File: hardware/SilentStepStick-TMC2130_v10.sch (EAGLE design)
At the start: 26 parts, among them IC1 TMC2100-LA, X1 PASSER-07, X2 PASSER-07

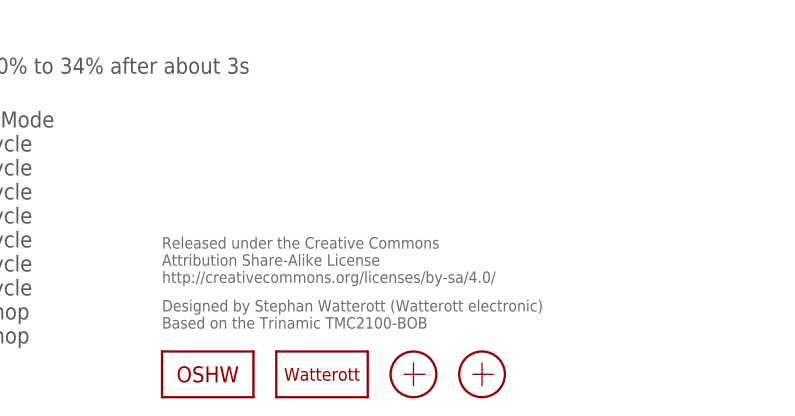
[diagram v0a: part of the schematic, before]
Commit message: updated schematics
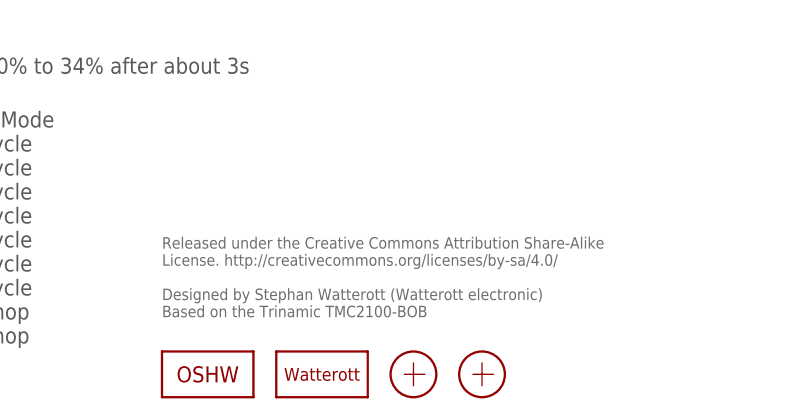
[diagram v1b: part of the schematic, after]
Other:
- note added: "Released under the Creative Commons Attribution Share-Alike License. http://creativecommons.org/licenses/by-sa/4.0/ Designed by Stephan Watterott (Watterott electronic) Based on the Trinamic TMC2100-BOB"
- note removed: "Designed by Stephan Watterott (Watterott electronic) Based on the Trinamic TMC2100-BOB"
- note removed: "Released under the Creative Commons Attribution Share-Alike License http://creativecommons.org/licenses/by-sa/4.0/"
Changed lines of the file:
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@@
 <setting verticaltext="up"/>
 </settings>
-<grid distance="0.1" unitdist="inch" unit="inch" style="lines" multiple="1" display="no" altdistance="0.01" altunitdist="inch" altunit="inch"/>
+<grid distance="0.05" unitdist="inch" unit="inch" style="lines" multiple="1" display="yes" altdistance="0.025" altunitdist="inch" altunit="inch"/>
 <layers>
 <layer number="1" name="Top" color="4" fill="1" visible="no" active="no"/>
@@
 <wire x1="38.1" y1="40.64" x2="38.1" y2="43.18" width="1.016" layer="94"/>
 <wire x1="38.1" y1="25.4" x2="38.1" y2="27.94" width="1.016" layer="94"/>
-<text x="162.56" y="17.78" size="1.27" layer="95">Released under the Creative Commons
-Attribution Share-Alike License
-http://creativecommons.org/licenses/by-sa/4.0/</text>
-<text x="162.56" y="12.7" size="1.27" layer="95">Designed by Stephan Watterott (Watterott electronic)
+<text x="162.56" y="22.86" size="1.27" layer="95" align="top-left">Released under the Creative Commons Attribution Share-Alike
+License. http://creativecommons.org/licenses/by-sa/4.0/
+Designed by Stephan Watterott (Watterott electronic)
 Based on the Trinamic TMC2100-BOB</text>
 <text x="90.17" y="50.8" size="1.778" layer="97" font="vector" ratio="10" align="top-left">CFG6/En
